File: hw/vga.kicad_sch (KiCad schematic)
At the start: 19 parts, among them J1 Conn_02x05_Odd_Even, J2 DB15_Female_HighDensity_Mount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, U1 74HC4053, U2 23LCV512, U3 ICS501

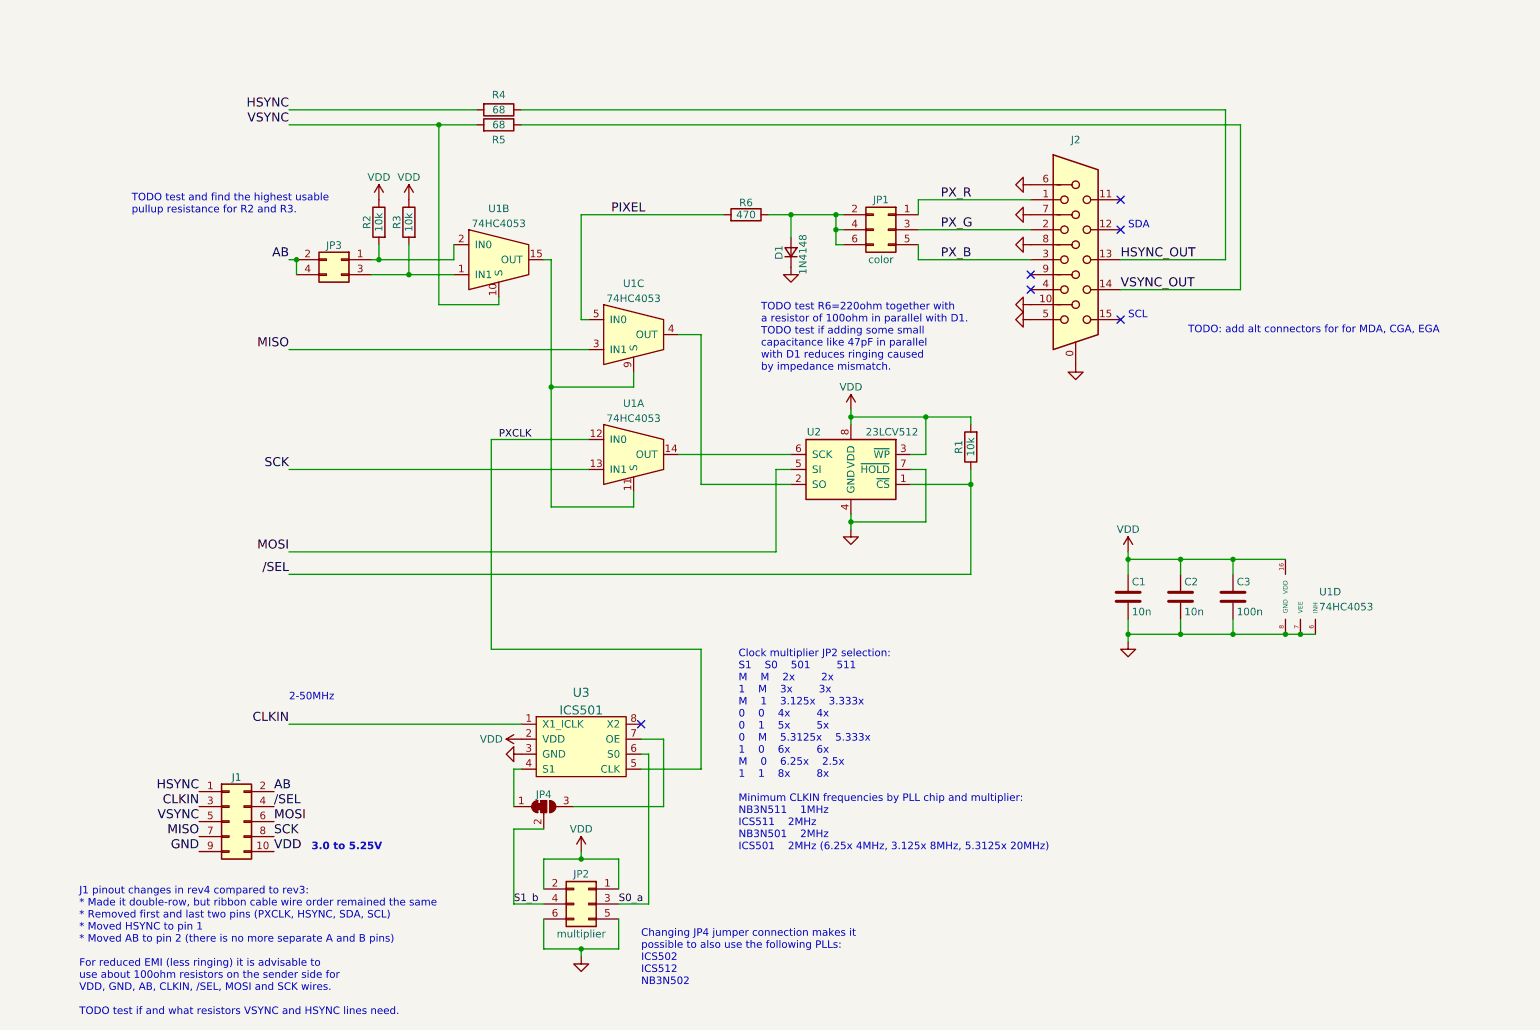
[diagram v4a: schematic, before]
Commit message: Cleaned up the schematic and changed some resistor values for better impedance matching
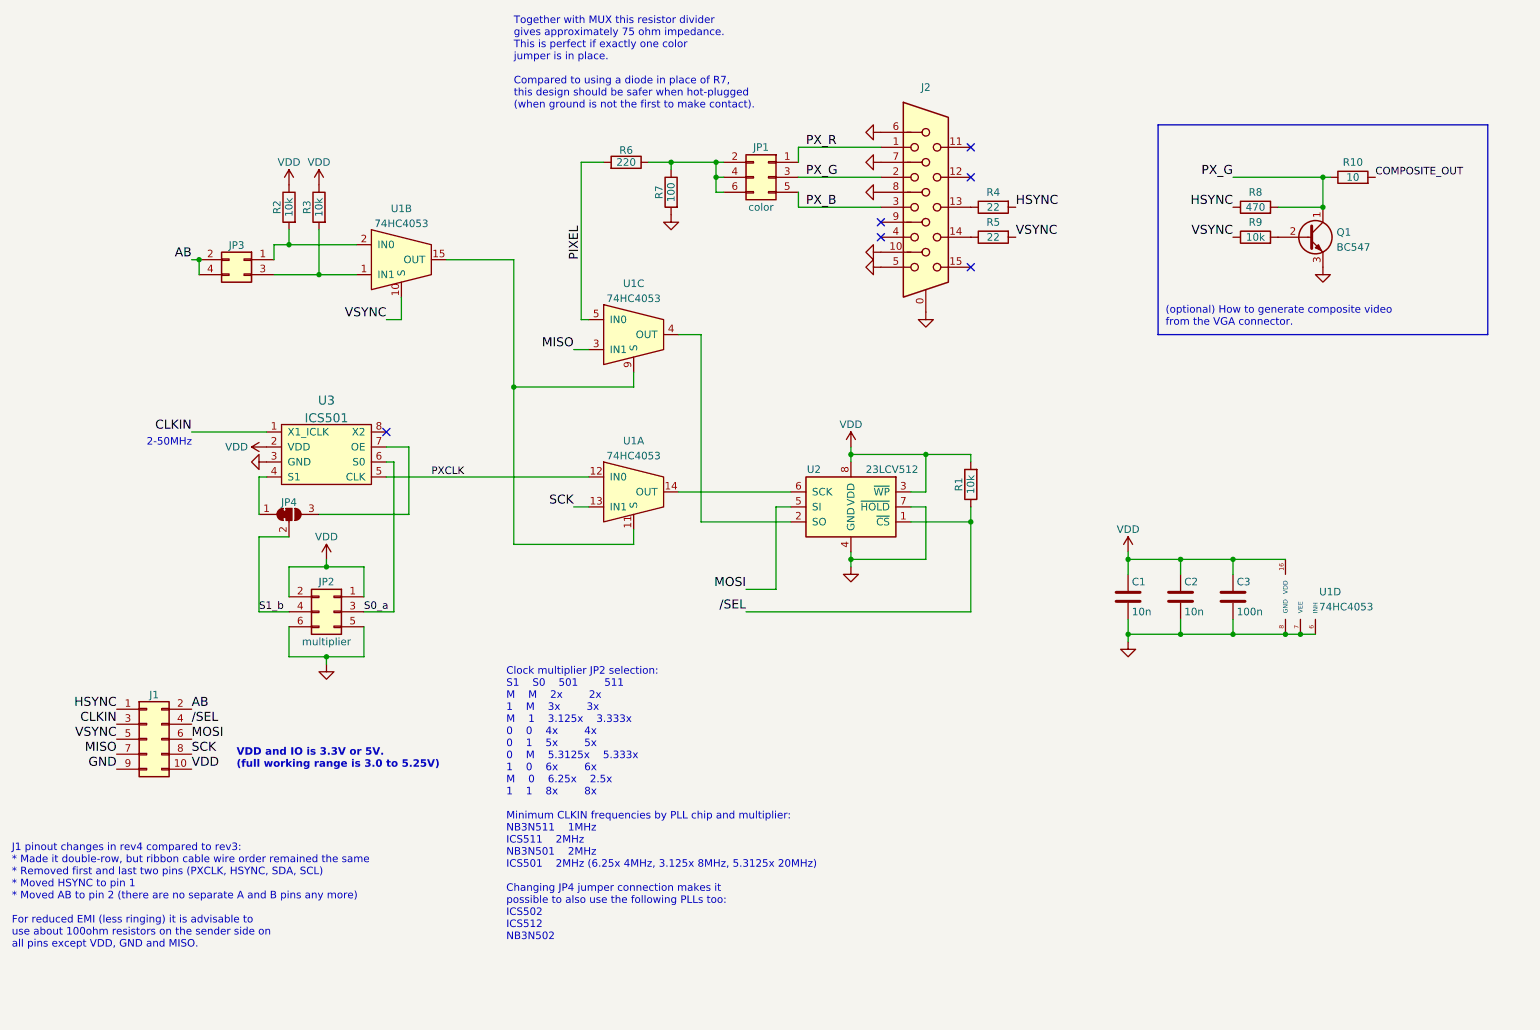
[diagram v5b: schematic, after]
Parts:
- removed D1: 1N4148, Diode_SMD:D_SOD-123, symbol Device:D_Small
- added Q1: BC547, symbol Transistor_BJT:BC547
- added R10: 10, symbol Device:R
- added R7: 100, Resistor_SMD:R_0805_2012Metric, symbol Device:R
- added R8: 470, symbol Device:R
- added R9: 10k, symbol Device:R
- R4, R5: value 68 -> 22
- R6: value 470 -> 220
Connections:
- net GND: now also Q1.3 (E), R7.2
- net HSYNC: now also R8.1
- net PX_G: now also Q1.1 (C), R10.1, R8.2
- net VSYNC: now also R9.1
- net at JP1.2 (Pin_2), JP1.4 (Pin_4), JP1.6 (Pin_6)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: now also R7.1
- net HSYNC_OUT: no longer names the net of J2.13, R4.1
- net VSYNC_OUT: no longer names the net of J2.14, R5.1
- new net: Q1.2 (B), R9.2
- new net COMPOSITE_OUT: R10.2
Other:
- note added: "(optional) How to generate composite video from the VGA connector."
- note added: "Clock multiplier JP2 selection: S1 S0 501 511 M M 2x 2x 1 M 3x 3x M 1 3.125x 3.333x 0 0 4x 4x 0 1 5x 5x 0 M 5.3125x 5.333x 1 0 6x 6x M 0 6.25x 2.5x 1 1 8x 8x Minimum CLKIN frequencies by PLL chip and multiplier: NB3N511 1MHz ICS511 2MHz NB3N501 2MHz ICS501 2MHz (6.25x 4MHz, 3.125x 8MHz, 5.3125x 20MHz) Changing JP4 jumper connection makes it possible to also use the following PLLs too: ICS502 ICS5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"
- note added: "J1 pinout changes in rev4 compared to rev3: * Made it double-row, but ribbon cable wire order remained the same * Removed first and last two pins (PXCLK, HSYNC, SDA, SCL) * Moved HSYNC to pin 1 * Moved AB to pin 2 (there are no separate A and B pins any more) For reduced EMI (less ringing) it is advisable to use about 100ohm resistors on the sender side on all pins except VDD, GND and MISO."
- note added: "Together with MUX this resistor divider gives approximately 75 ohm impedance. This is perfect if exactly one color jumper is in place. Compared to using a diode in place of R7, this design should be safer when hot-plugged (when ground is not the first to make contact)."
- note added: "VDD and IO is 3.3V or 5V. (full working range is 3.0 to 5.25V)"
- note removed: "3.0 to 5.25V"
- note removed: "Changing JP4 jumper connection makes it possible to also use the following PLLs: ICS502 ICS512 NB3N502"
- note removed: "Clock multiplier JP2 selection: S1 S0 501 511 M M 2x 2x 1 M 3x 3x M 1 3.125x 3.333x 0 0 4x 4x 0 1 5x 5x 0 M 5.3125x 5.333x 1 0 6x 6x M 0 6.25x 2.5x 1 1 8x 8x Minimum CLKIN frequencies by PLL chip and multiplier: NB3N511 1MHz ICS511 2MHz NB3N501 2MHz ICS501 2MHz (6.25x 4MHz, 3.125x 8MHz, 5.3125x 20MHz)"
- note removed: "J1 pinout changes in rev4 compared to rev3: * Made it double-row, but ribbon cable wire order remained the same * Removed first and last two pins (PXCLK, HSYNC, SDA, SCL) * Moved HSYNC to pin 1 * Moved AB to pin 2 (there is no more separate A and B pins) For reduced EMI (less ringing) it is advisable to use about 100ohm resistors on the sender side for VDD, GND, AB, CLKIN, /SEL, MOSI and SCK wire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"
- note removed: "SCL"
- note removed: "SDA"
- note removed: "TODO test R6=220ohm together with a resistor of 100ohm in parallel with D1. TODO test if adding some small capacitance like 47pF in parallel with D1 reduces ringing caused by impedance mismatch."
- note removed: "TODO test and find the highest usable pullup resistance for R2 and R3."
- note removed: "TODO: add alt connectors for for MDA, CGA, EGA"
- moved on the sheet: J1, J2, JP1, JP2, JP3, JP4, R1, R2, R3, R4, R5, R6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
